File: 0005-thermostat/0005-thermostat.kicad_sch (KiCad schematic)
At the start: 45 parts, among them J1 EXT_NTC, J2 OUT, J3 PWR, J4 EXT_LED, J5 EXT_P1, J6 EXT_P2, P1 22k, P2 22k, T1 BC847B, T2 BC847B, T3 BC847B

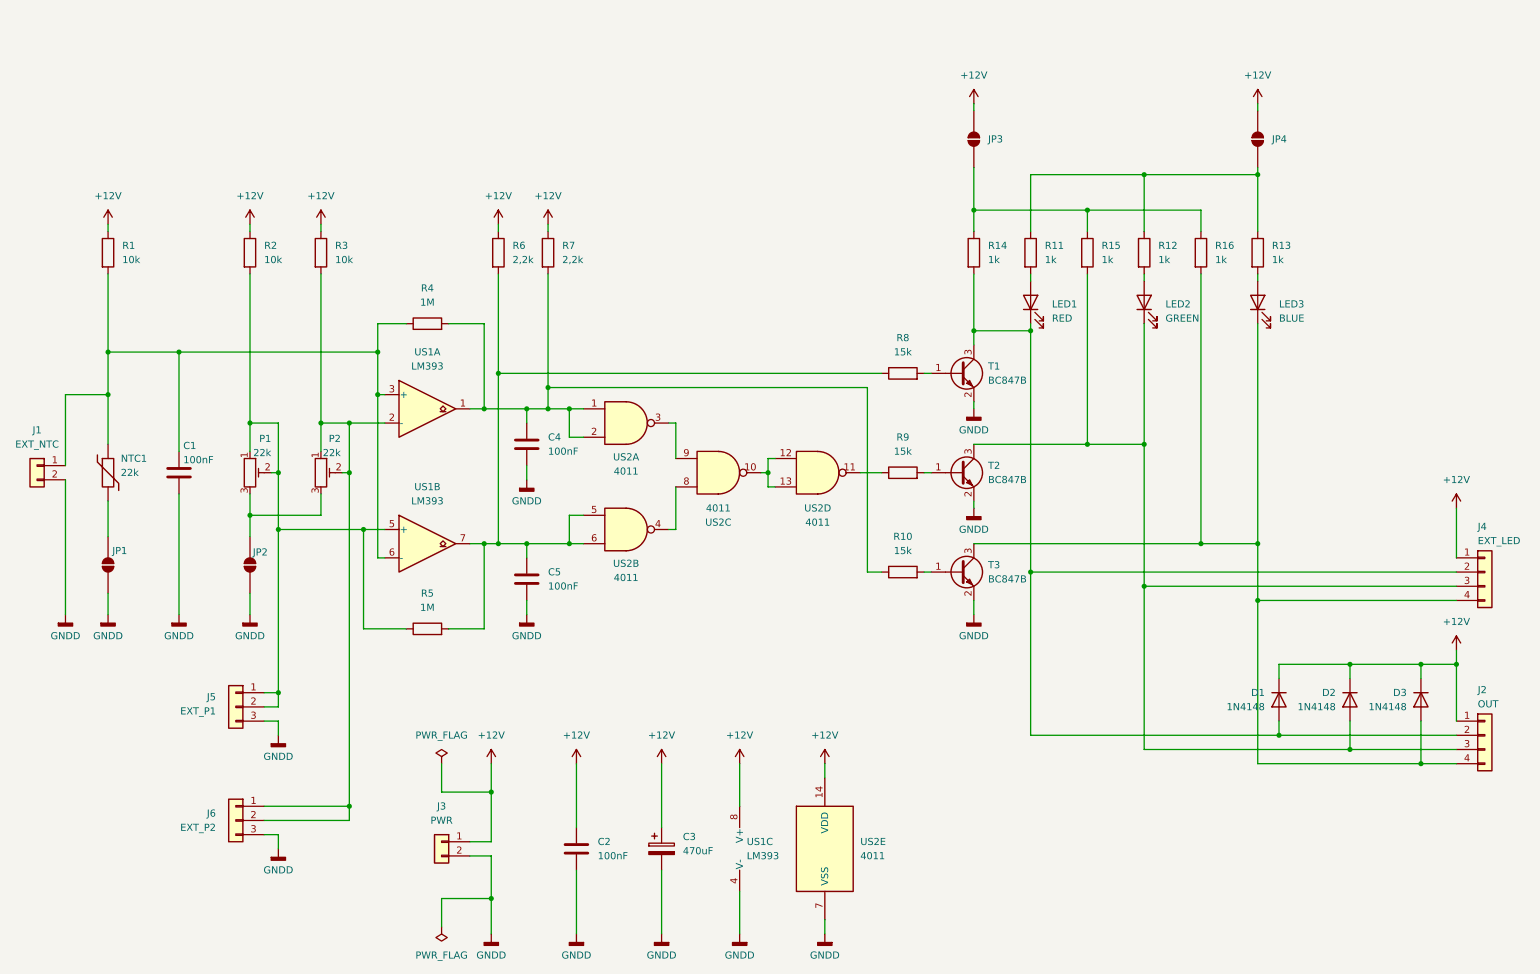
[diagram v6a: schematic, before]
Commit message: Initial documentation (#2)
* Initial documentation
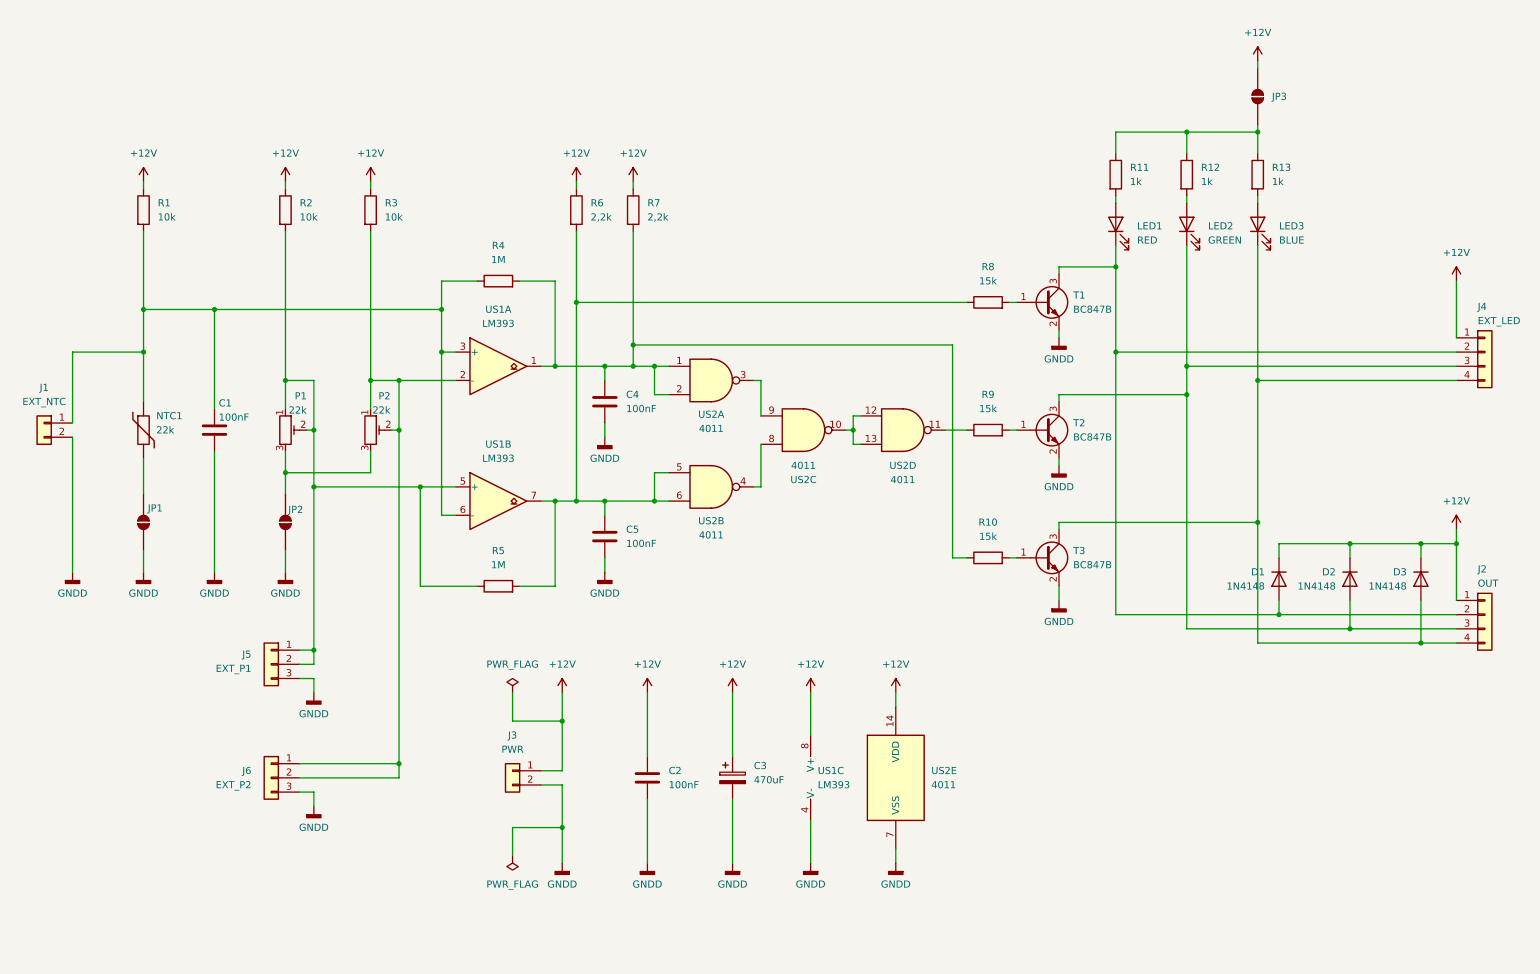
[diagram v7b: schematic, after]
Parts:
- removed JP3: SolderJumper_2_Open, symbol Jumper:SolderJumper_2_Open
- removed R14, R15, R16: 1k, symbol Device:R
- renumbered JP4 to JP3
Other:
- moved on the sheet: C1, C2, C3, C4, C5, D1, D2, D3, J1, J2, J3, J4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

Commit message: Assign footprints, generate BOMs (#3)
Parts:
- C1, C2, C4, C5: footprint (none) -> Capacitor_SMD:C_0603_1608Metric_Pad1.08x0.95mm_HandSolder
- C3: footprint (none) -> Capacitor_SMD:CP_Elec_10x10
- J1, J3: footprint (none) -> Connector_JST:JST_SH_BM02B-SRSS-TB_1x02-1MP_P1.00mm_Vertical
- J2, J4: footprint (none) -> Connector_JST:JST_SH_BM04B-SRSS-TB_1x04-1MP_P1.00mm_Vertical
- J5, J6: footprint (none) -> Connector_JST:JST_SH_BM03B-SRSS-TB_1x03-1MP_P1.00mm_Vertical
- JP1, JP2, JP3: footprint (none) -> Jumper:SolderJumper-2_P1.3mm_Open_Pad1.0x1.5mm
- LED1, LED2, LED3: footprint (none) -> LED_SMD:LED_0603_1608Metric_Pad1.05x0.95mm_HandSolder
- NTC1, R1, R10, R11, R12, R2, R3, R4, R5, R6, R7, R8, R9: footprint (none) -> Resistor_SMD:R_0603_1608Metric_Pad0.98x0.95mm_HandSolder
- P1, P2: footprint (none) -> Potentiometer_SMD:Potentiometer_Bourns_3224W_Vertical
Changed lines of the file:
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@@
 			)
 		)
-		(property "Footprint" ""
+		(property "Footprint" "Capacitor_SMD:C_0603_1608Metric_Pad1.08x0.95mm_HandSolder"
 			(at 120.3452 88.9 0)
 			(hide yes)
@@
 			)
 		)
-		(property "Footprint" ""
+		(property "Footprint" "Resistor_SMD:R_0603_1608Metric_Pad0.98x0.95mm_HandSolder"
 			(at 187.96 69.088 90)
 			(hide yes)
@@
 			)
 		)
-		(property "Footprint" ""
+		(property "Footprint" "Resistor_SMD:R_0603_1608Metric_Pad0.98x0.95mm_HandSolder"
 			(at 60.452 50.8 90)
 			(hide yes)
@@
 			)
 		)
-		(property "Footprint" ""
+		(property "Footprint" "Jumper:SolderJumper-2_P1.3mm_Open_Pad1.0x1.5mm"
 			(at 62.23 106.68 0)
 			(hide yes)
@@
 			)
 		)
-		(property "Footprint" ""
+		(property "Footprint" "Capacitor_SMD:C_0603_1608Metric_Pad1.08x0.95mm_HandSolder"
 			(at 127.9652 156.21 0)
 			(hide yes)
@@
 			)
 		)
-		(property "Footprint" ""
+		(property "Footprint" "LED_SMD:LED_0603_1608Metric_Pad1.05x0.95mm_HandSolder"
 			(at 236.22 53.34 0)
 			(hide yes)
@@
 			)
 		)
-		(property "Footprint" ""
+		(property "Footprint" "Resistor_SMD:R_0603_1608Metric_Pad0.98x0.95mm_HandSolder"
 			(at 187.96 114.808 90)
 			(hide yes)
@@
 			)
 		)
-		(property "Footprint" ""
+		(property "Footprint" "Resistor_SMD:R_0603_1608Metric_Pad0.98x0.95mm_HandSolder"
 			(at 122.682 50.8 90)
 			(hide yes)
@@
 			)
 		)
-		(property "Footprint" ""
+		(property "Footprint" "LED_SMD:LED_0603_1608Metric_Pad1.05x0.95mm_HandSolder"
 			(at 223.52 53.34 0)
 			(hide yes)
@@
 			)
 		)
-		(property "Footprint" ""
+		(property "Footprint" "Potentiometer_SMD:Potentiometer_Bourns_3224W_Vertical"
 			(at 77.47 90.17 0)
 			(hide yes)
@@
 			)
 		)
-		(property "Footprint" ""
+		(property "Footprint" "Resistor_SMD:R_0603_1608Metric_Pad0.98x0.95mm_HandSolder"
 			(at 221.742 44.45 90)
 			(hide yes)
@@
 			)
 		)
-		(property "Footprint" ""
+		(property "Footprint" "Connector_JST:JST_SH_BM03B-SRSS-TB_1x03-1MP_P1.00mm_Vertical"
 			(at 59.69 132.08 0)
 			(hide yes)
@@
 			)
 		)
-		(property "Footprint" ""
+		(property "Footprint" "Connector_JST:JST_SH_BM04B-SRSS-TB_1x04-1MP_P1.00mm_Vertical"
 			(at 276.86 76.2 0)
 			(hide yes)
@@
 			)
 		)
-		(property "Footprint" ""
+		(property "Footprint" "Resistor_SMD:R_0603_1608Metric_Pad0.98x0.95mm_HandSolder"
 			(at 100.33 119.888 90)
 			(hide yes)
@@
 			)
 		)
-		(property "Footprint" ""
+		(property "Footprint" "Jumper:SolderJumper-2_P1.3mm_Open_Pad1.0x1.5mm"
 			(at 36.83 106.68 0)
 			(hide yes)
@@
 			)
 		)
-		(property "Footprint" ""
+		(property "Footprint" "Resistor_SMD:R_0603_1608Metric_Pad0.98x0.95mm_HandSolder"
 			(at 100.33 65.278 90)
 			(hide yes)
@@
 			)
 		)
-		(property "Footprint" ""
+		(property "Footprint" "Resistor_SMD:R_0603_1608Metric_Pad0.98x0.95mm_HandSolder"
 			(at 112.522 50.8 90)
 			(hide yes)
@@
 			)
 		)
-		(property "Footprint" ""
+		(property "Footprint" "Capacitor_SMD:C_0603_1608Metric_Pad1.08x0.95mm_HandSolder"
 			(at 120.3452 113.03 0)
 			(hide yes)
@@
 			)
 		)
-		(property "Footprint" ""
+		(property "Footprint" "Connector_JST:JST_SH_BM03B-SRSS-TB_1x03-1MP_P1.00mm_Vertical"
 			(at 59.69 152.4 0)
 			(hide yes)
@@
 			)
 		)
-		(property "Footprint" ""
+		(property "Footprint" "Capacitor_SMD:CP_Elec_10x10"
 			(at 143.2052 156.21 0)
 			(hide yes)
@@
 			)
 		)
-		(property "Footprint" ""
+		(property "Footprint" "LED_SMD:LED_0603_1608Metric_Pad1.05x0.95mm_HandSolder"
 			(at 210.82 53.34 0)
 			(hide yes)
@@
 			)
 		)
-		(property "Footprint" ""
+		(property "Footprint" "Connector_JST:JST_SH_BM02B-SRSS-TB_1x02-1MP_P1.00mm_Vertical"
 			(at 102.87 151.13 0)
 			(hide yes)
@@
 			)
 		)
-		(property "Footprint" ""
+		(property "Footprint" "Capacitor_SMD:C_0603_1608Metric_Pad1.08x0.95mm_HandSolder"
 			(at 50.4952 93.98 0)
 			(hide yes)
@@
 			)
 		)
-		(property "Footprint" ""
+		(property "Footprint" "Resistor_SMD:R_0603_1608Metric_Pad0.98x0.95mm_HandSolder"
 			(at 75.692 50.8 90)
 			(hide yes)
@@
 			)
 		)
-		(property "Footprint" ""
+		(property "Footprint" "Connector_JST:JST_SH_BM04B-SRSS-TB_1x04-1MP_P1.00mm_Vertical"
 			(at 276.86 123.19 0)
 			(hide yes)
@@
 			)
 		)
-		(property "Footprint" ""
+		(property "Footprint" "Resistor_SMD:R_0603_1608Metric_Pad0.98x0.95mm_HandSolder"
 			(at 209.042 44.45 90)
 			(hide yes)
@@
 			)
 		)
-		(property "Footprint" ""
+		(property "Footprint" "Connector_JST:JST_SH_BM02B-SRSS-TB_1x02-1MP_P1.00mm_Vertical"
 			(at 19.05 88.9 0)
 			(hide yes)
@@
 			)
 		)
-		(property "Footprint" ""
+		(property "Footprint" "Resistor_SMD:R_0603_1608Metric_Pad0.98x0.95mm_HandSolder"
 			(at 35.052 50.8 90)
 			(hide yes)
@@
 			)
 		)
-		(property "Footprint" ""
+		(property "Footprint" "Potentiometer_SMD:Potentiometer_Bourns_3224W_Vertical"
 			(at 62.23 90.17 0)
 			(hide yes)
@@
 			)
 		)
-		(property "Footprint" ""
+		(property "Footprint" "Resistor_SMD:R_0603_1608Metric_Pad0.98x0.95mm_HandSolder"
 			(at 187.96 91.948 90)
 			(hide yes)
@@
 			)
 		)
-		(property "Footprint" ""
+		(property "Footprint" "Resistor_SMD:R_0603_1608Metric_Pad0.98x0.95mm_HandSolder"
 			(at 36.83 90.17 0)
 			(hide yes)
@@
 			)
 		)
-		(property "Footprint" ""
+		(property "Footprint" "Jumper:SolderJumper-2_P1.3mm_Open_Pad1.0x1.5mm"
 			(at 236.22 30.48 0)
 			(hide yes)
